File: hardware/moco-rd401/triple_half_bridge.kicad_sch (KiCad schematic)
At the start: 66 parts, among them J6 U, J7 V, J8 W

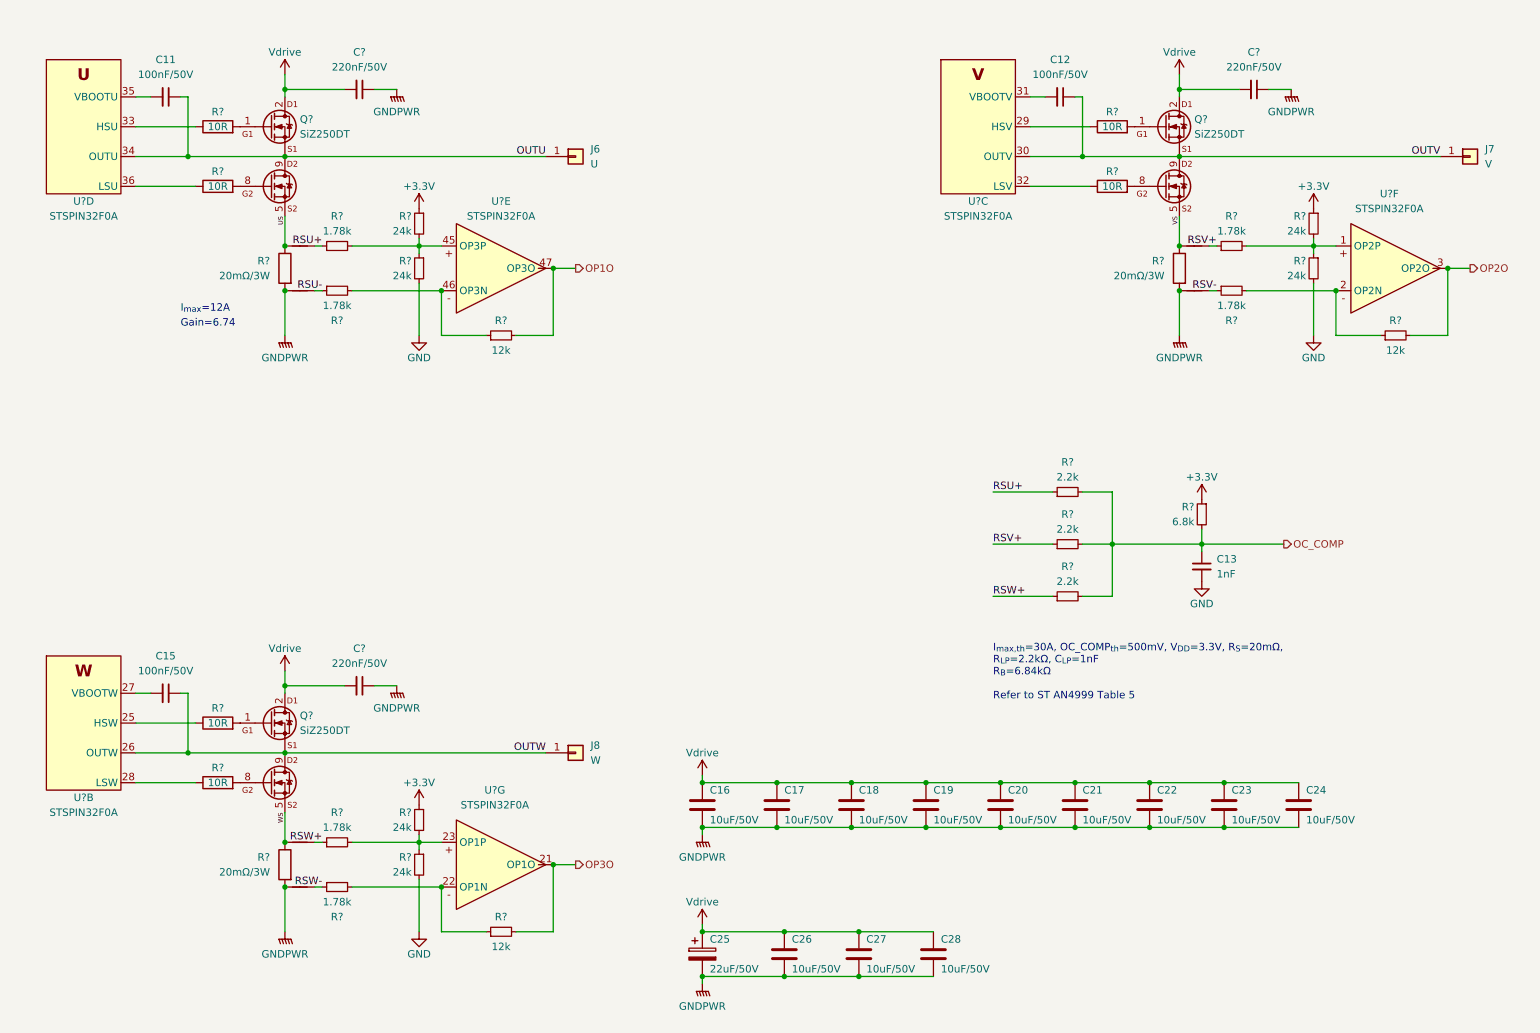
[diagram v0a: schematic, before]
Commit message: Rename power stage to triple half bridge
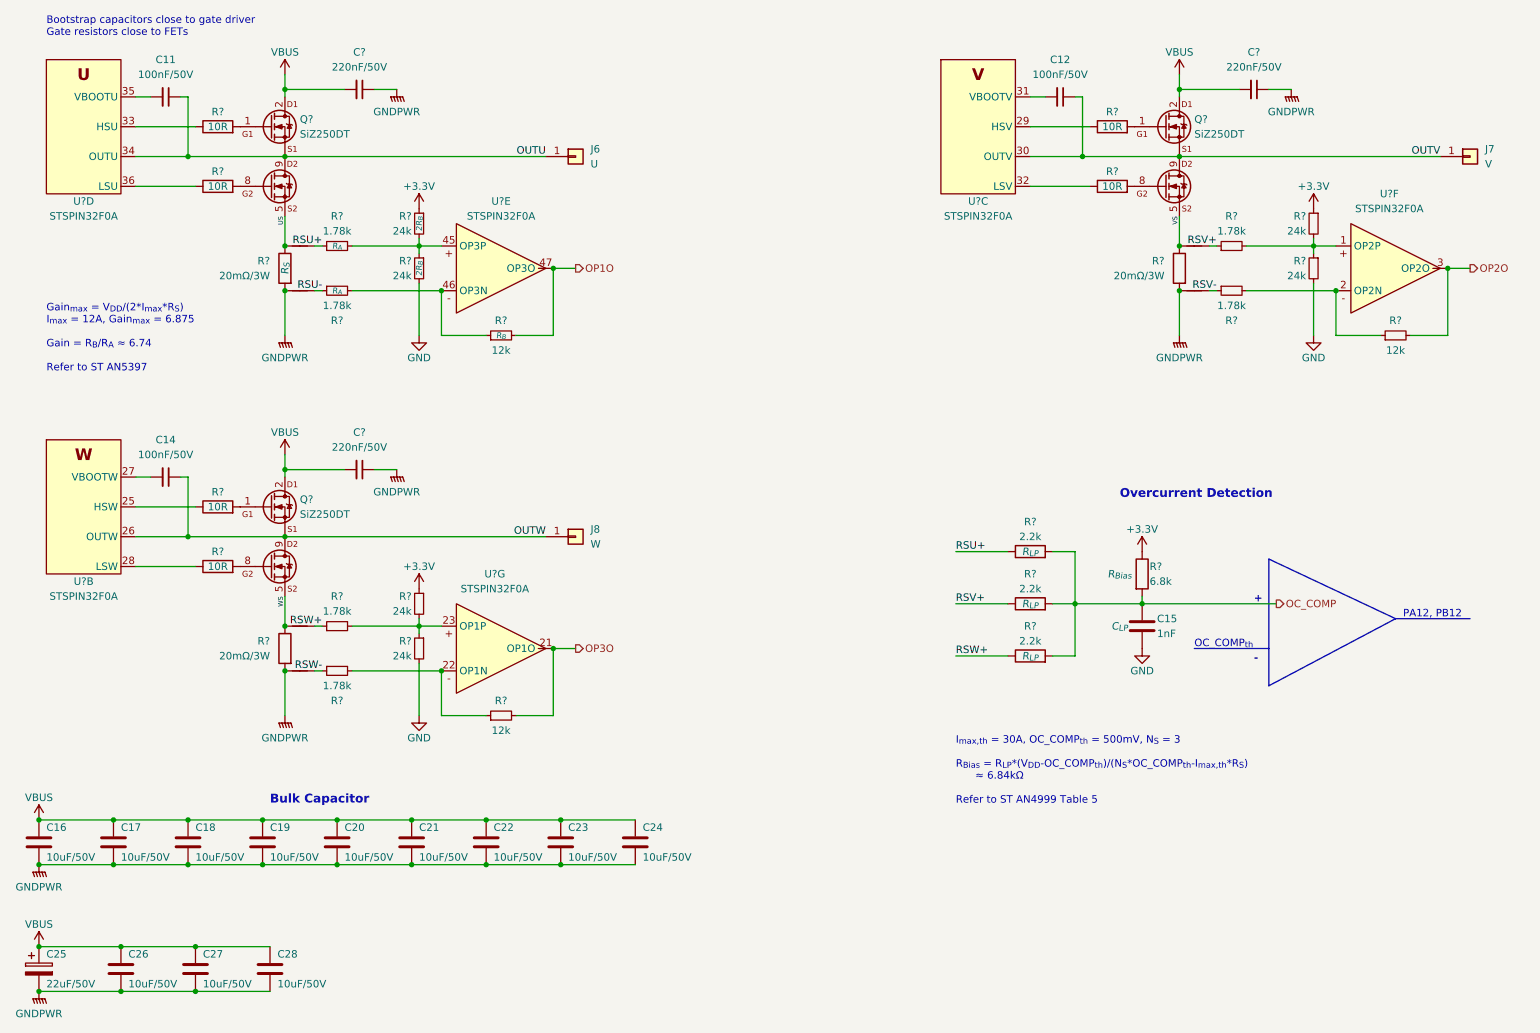
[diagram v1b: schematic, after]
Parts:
- C15: renamed from C13; symbol Device:C_Small -> Device:C; Note (none) -> C_{LP}
- R?: Note (none) -> R_{S}
- R? (x3): symbol Device:R_Small -> Device:R; Note (none) -> R_{LP}
- R? (x2): Note (none) -> 2R_{B}
- R?: Note (none) -> R_{B}
- R? (x2): Note (none) -> R_{A}
- R?: symbol Device:R_Small -> Device:R; Note (none) -> R_{Bias}
- renumbered C15 to C14
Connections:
- net Vdrive renamed VBUS
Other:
- note added: "+"
- note added: "-"
- note added: "Bootstrap capacitors close to gate driver Gate resistors close to FETs"
- note added: "Bulk Capacitor"
- note added: "Gain_{max} = V_{DD}/(2*I_{max}*R_{S}) I_{max} = 12A, Gain_{max} = 6.875 Gain = R_{B}/R_{A} ≈ 6.74 Refer to ST AN5397"
- note added: "I_{max,th} = 30A, OC_COMP_{th} = 500mV, N_{S} = 3 R_{Bias} = R_{LP}*(V_{DD}-OC_COMP_{th})/(N_{S}*OC_COMP_{th}-I_{max,th}*R_{S}) ≈ 6.84kΩ Refer to ST AN4999 Table 5"
- note added: "OC_COMP_{th}"
- note added: "Overcurrent Detection"
- note added: "PA12, PB12"
- note removed: "Gain=6.74"
- note removed: "I_{max,th}=30A, OC_COMP_{th}=500mV, V_{DD}=3.3V, R_{S}=20mΩ, R_{LP}=2.2kΩ, C_{LP}=1nF R_{B}=6.84kΩ Refer to ST AN4999 Table 5"
- note removed: "I_{max}=12A"
- moved on the sheet: C14, C15, C16, C17, C18, C19, C20, C21, C22, C23, C24, C25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
